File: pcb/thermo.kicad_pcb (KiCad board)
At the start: 2 copper layers, 123.2 x 91.4 mm, 38 parts, among them J1 DB15_Female, J2 Barrel_Jack, U1 BME280

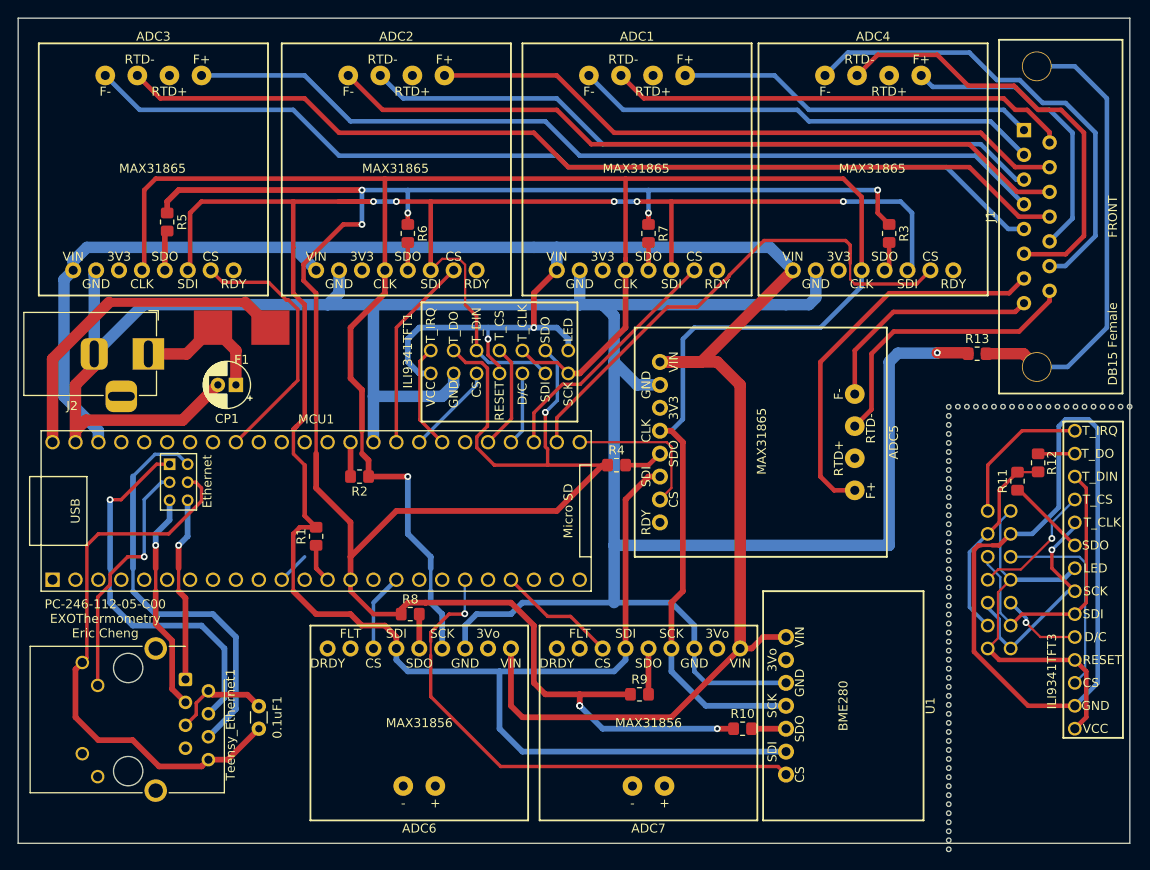
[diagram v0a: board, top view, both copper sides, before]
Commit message: fixed MAX31865 sensor side pinout mixup, new layout on OSHPark V2
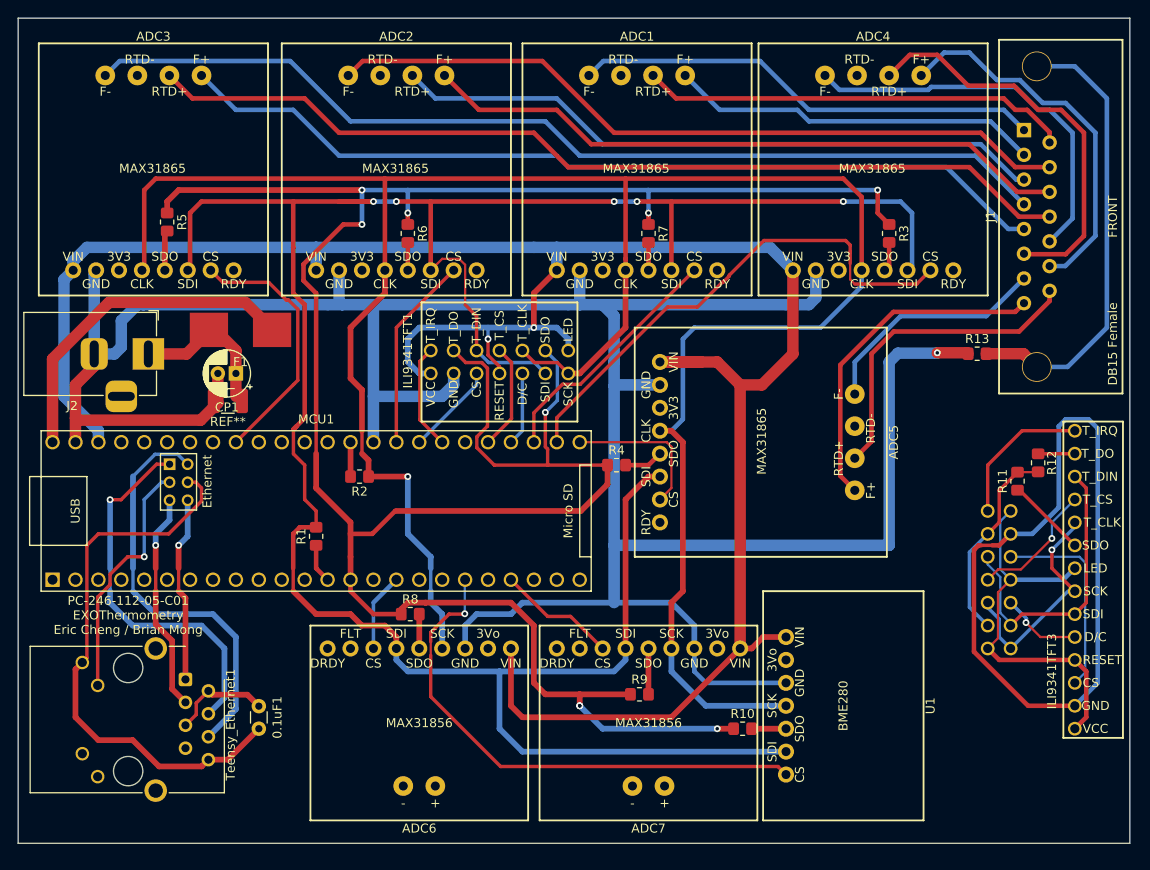
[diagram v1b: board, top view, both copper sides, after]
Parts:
- removed the REF** at (120.9, 148.6)
- removed the REF** at (120.9, 138.6)
- removed the REF** at (120.9, 128.5)
- removed the REF** at (120.9, 118.5)
- removed the REF** at (120.9, 108.5)
- removed the REF** at (126.4, 104.0)
- removed the REF** at (136.4, 104.0)
- added REF**: breakoff, Thermometry:breakoff, F.Cu at (121.0, 151.3)
- added REF**: breakoff, Thermometry:breakoff, F.Cu at (121.0, 132.5)
- added REF**: breakoff, Thermometry:breakoff, F.Cu at (121.0, 130.3)
- added REF**: breakoff, Thermometry:breakoff, F.Cu at (121.0, 128.3)
- added REF**: breakoff, Thermometry:breakoff, F.Cu at (121.0, 126.1)
- added REF**: breakoff, Thermometry:breakoff, F.Cu at (121.0, 124.1)
- added REF**: breakoff, Thermometry:breakoff, F.Cu at (121.0, 121.9)
- added REF**: breakoff, Thermometry:breakoff, F.Cu at (121.0, 119.9)
- added REF**: breakoff, Thermometry:breakoff, F.Cu at (121.0, 117.7)
- added REF**: breakoff, Thermometry:breakoff, F.Cu at (121.0, 115.7)
- added REF**: breakoff, Thermometry:breakoff, F.Cu at (121.0, 113.5)
- added REF**: breakoff, Thermometry:breakoff, F.Cu at (121.0, 149.2)
- added REF**: breakoff, Thermometry:breakoff, F.Cu at (121.0, 111.5)
- added REF**: breakoff, Thermometry:breakoff, F.Cu at (121.0, 109.3)
- added REF**: breakoff, Thermometry:breakoff, F.Cu at (121.0, 107.3)
- added REF**: breakoff, Thermometry:breakoff, F.Cu at (121.0, 105.2)
- added REF**: breakoff, Thermometry:breakoff, F.Cu at (139.4, 104.0)
- added REF**: breakoff, Thermometry:breakoff, F.Cu at (137.2, 104.0)
- added REF**: breakoff, Thermometry:breakoff, F.Cu at (135.0, 104.0)
- added REF**: breakoff, Thermometry:breakoff, F.Cu at (132.8, 104.0)
- added REF**: breakoff, Thermometry:breakoff, F.Cu at (130.8, 104.0)
- added REF**: breakoff, Thermometry:breakoff, F.Cu at (128.7, 104.0)
- added REF**: breakoff, Thermometry:breakoff, F.Cu at (121.0, 147.1)
- added REF**: breakoff, Thermometry:breakoff, F.Cu at (126.6, 104.0)
- added REF**: breakoff, Thermometry:breakoff, F.Cu at (124.5, 104.0)
- added REF**: breakoff, Thermometry:breakoff, F.Cu at (122.3, 104.0)
- added REF**: C_1210_3225Metric_Pad1.33x2.70mm_HandSolder, Capacitor_SMD:C_1210_3225Metric_Pad1.33x2.70mm_HandSolder, F.Cu at (41.0, 103.4)
- added REF**: breakoff, Thermometry:breakoff, F.Cu at (121.0, 145.0)
- added REF**: breakoff, Thermometry:breakoff, F.Cu at (121.0, 142.9)
- added REF**: breakoff, Thermometry:breakoff, F.Cu at (121.0, 140.8)
- added REF**: breakoff, Thermometry:breakoff, F.Cu at (121.0, 138.7)
- added REF**: breakoff, Thermometry:breakoff, F.Cu at (121.0, 136.7)
- added REF**: breakoff, Thermometry:breakoff, F.Cu at (121.0, 134.5)
- moved CP1 1.27 mm to (41.9, 100.3)
- moved F1 0.29 mm to (42.4, 95.5)
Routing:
- net Net-(ADC5-Pad12): track 43.5 -> 26.1 mm
- net Net-(ADC3-Pad12): track 97.1 -> 109.0 mm
- net Net-(ADC2-Pad12): track 71.3 -> 83.3 mm
- net Net-(ADC1-Pad12): track 40.1 -> 52.0 mm
- net Net-(ADC5-Pad9): track 25.8 -> 37.7 mm
- net Net-(ADC4-Pad12): track 32.5 -> 43.4 mm
- net Net-(ADC3-Pad9): track 108.9 -> 98.2 mm
- net Net-(ADC2-Pad9): track 83.2 -> 72.5 mm
- net Net-(ADC1-Pad9): track 51.9 -> 41.2 mm
- net Net-(ADC4-Pad9): track 52.6 -> 41.9 mm
- net Net-(MCU1-Pad11): track 3.59 -> 0.00 mm
- net Net-(ADC1-Pad10): track 51.2 -> 47.7 mm
- net Net-(ADC5-Pad10): track 32.5 -> 36.1 mm
- net Net-(ADC4-Pad10): track 48.6 -> 45.1 mm
- net Net-(ADC3-Pad10): track 107.7 -> 104.1 mm
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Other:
- board text added: "PC-246-112-05-C01 EXOThermometry Eric Cheng / Brian Mong"
- board text removed: "PC-246-112-05-C00 EXOThermometry Eric Cheng"
